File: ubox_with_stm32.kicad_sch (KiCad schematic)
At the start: 21 parts, among them J1 I2c_pin, J3 UART_Pin, U3 SAM-M10Q-00B

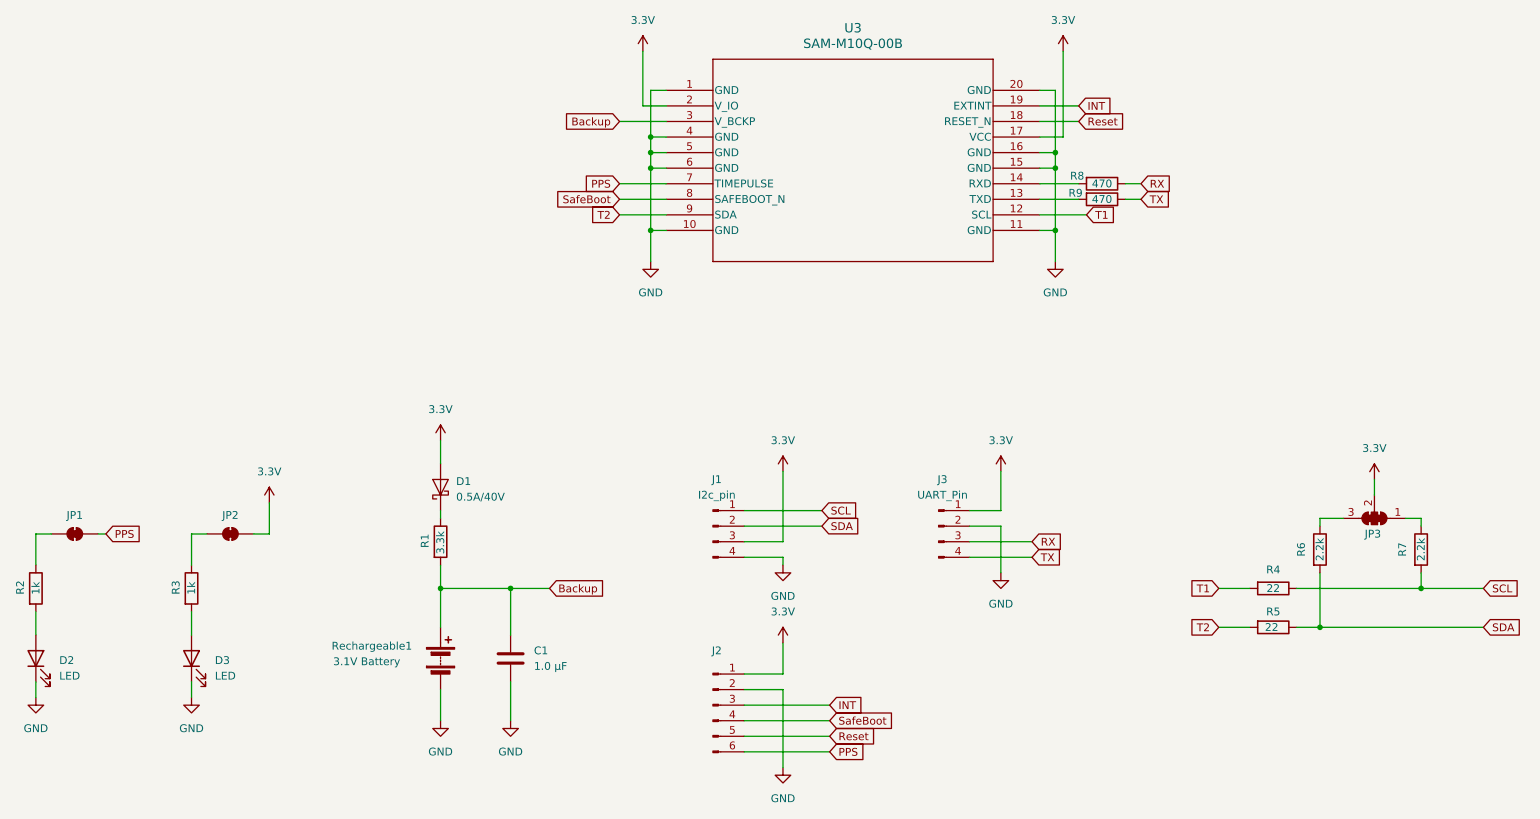
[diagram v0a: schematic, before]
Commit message: add decoupling
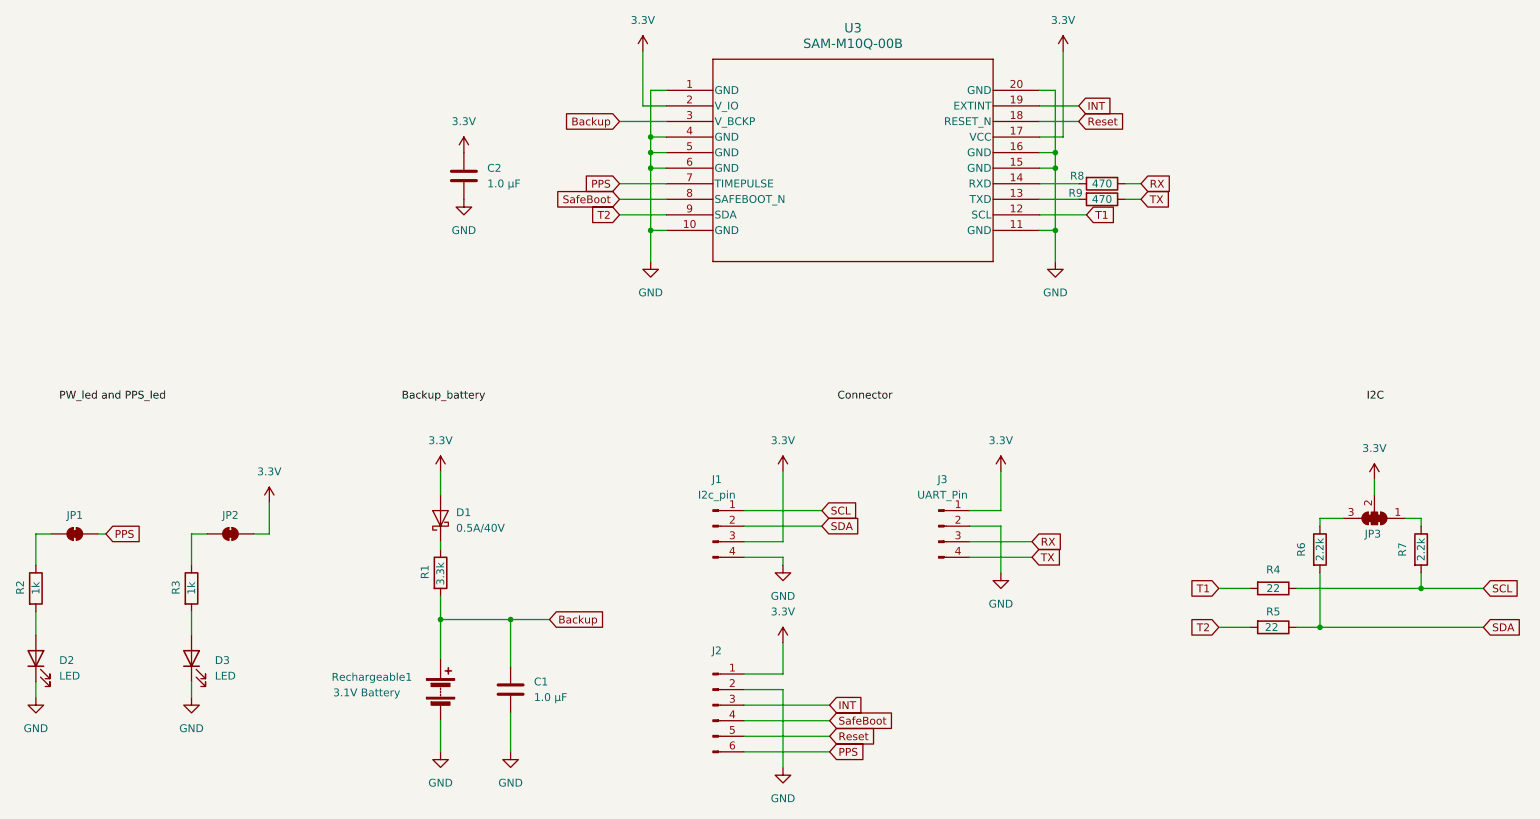
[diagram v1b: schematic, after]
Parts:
- added C2: 1.0 µF, Capacitor_SMD:C_0201_0603Metric, symbol Device:C
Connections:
- net 3.3V: now also C2.1
- net GND: now also C2.2
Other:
- moved on the sheet: C1, D1, R1, Rechargeable1
